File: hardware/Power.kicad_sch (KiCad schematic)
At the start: 1 part, among them J201 4090 USB-C

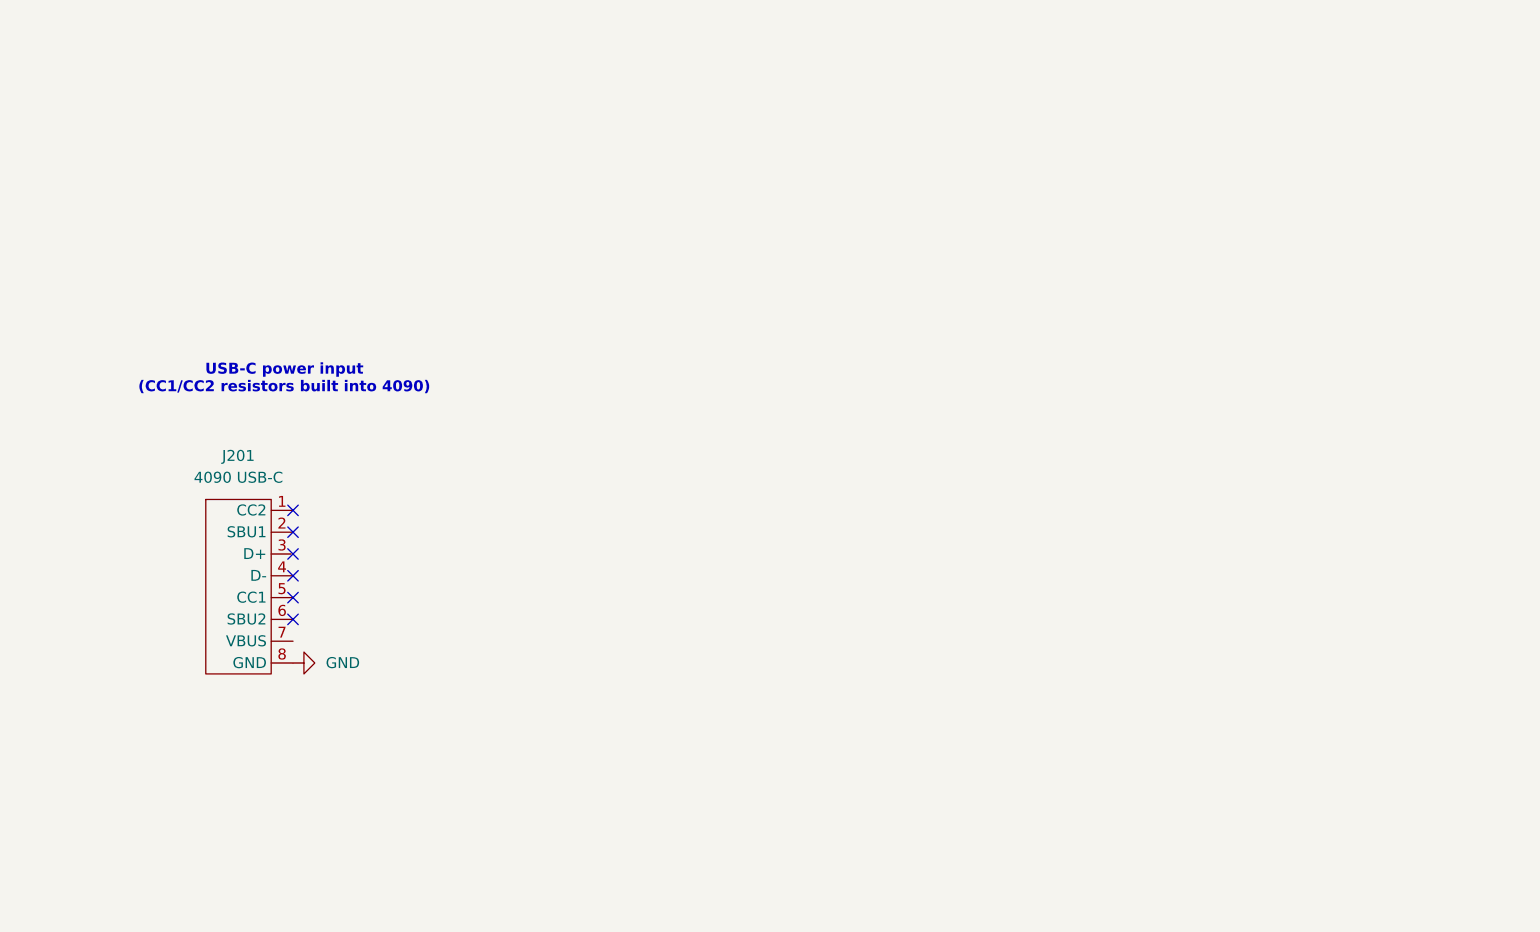
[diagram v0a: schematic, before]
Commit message: Complete schematics and component placements on board
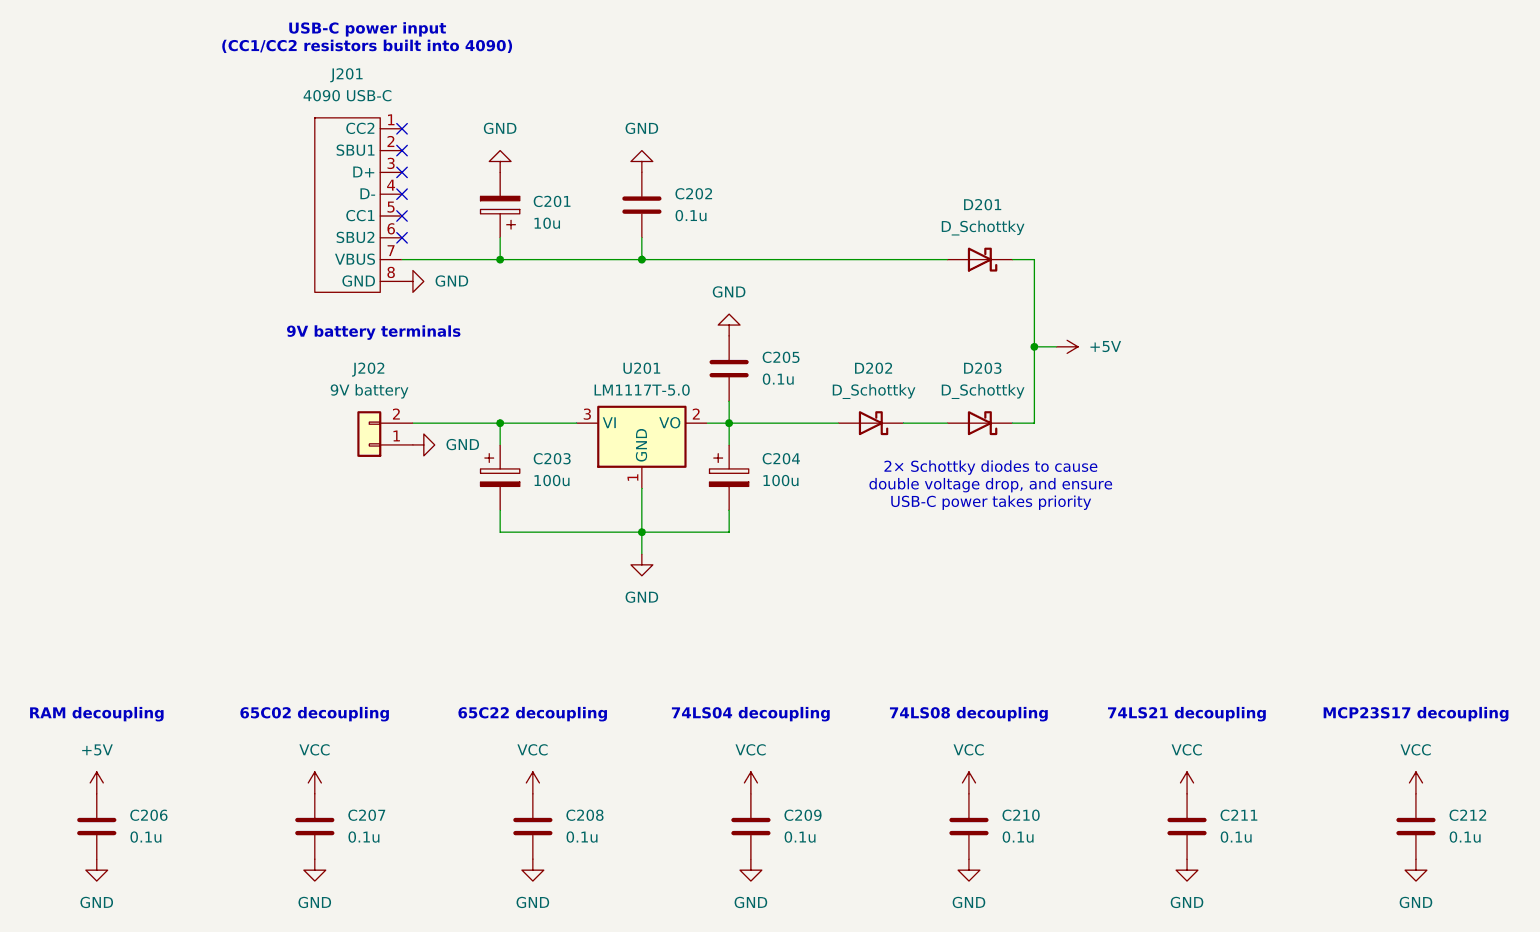
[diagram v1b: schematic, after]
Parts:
- added C201: 10u, Capacitor_THT:CP_Radial_D5.0mm_P2.00mm, symbol Device:C_Polarized
- added C202, C205, C206, C207, C208, C209, C210, C211, C212: 0.1u, Capacitor_THT:CP_Radial_D4.0mm_P1.50mm, symbol Device:C
- added C203, C204: 100u, Capacitor_THT:CP_Radial_D6.3mm_P2.50mm, symbol Device:C_Polarized
- added D201, D202, D203: D_Schottky, Diode_THT:D_DO-41_SOD81_P7.62mm_Horizontal, symbol Device:D_Schottky
- added J202: 9V battery, Connector_PinHeader_2.54mm:PinHeader_2x01_P2.54mm_Vertical, symbol Connector_Generic:Conn_01x02
- added U201: LM1117T-5.0, Package_TO_SOT_THT:TO-220-3_Horizontal_TabDown, symbol Regulator_Linear:LM1117T-5.0
- J201: footprint (none) -> Connector_PinHeader_2.54mm:PinHeader_1x08_P2.54mm_Vertical
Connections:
- net GND: now also C201.2, C202.1, C203.2, C204.2, C205.1, C206.2, C207.2, C208.2, C209.2, C210.2, C211.2, C212.2, J202.1 (Pin_1), U201.1 (GND)
- net at J201.7 (VBUS): now also C201.1, C202.2, D201.2 (A)
- new net: C203.1, J202.2 (Pin_2), U201.3 (VI)
- new net: D202.1 (K), D203.2 (A)
- new net: C204.1, C205.2, D202.2 (A), U201.2 (VO)
- new net +5V: C206.1, D201.1 (K), D203.1 (K)
- new net VCC: C207.1, C208.1, C209.1, C210.1, C211.1, C212.1
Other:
- note added: "2× Schottky diodes to cause double voltage drop, and ensure USB-C power takes priority"
- note added: "65C02 decoupling"
- note added: "65C22 decoupling"
- note added: "74LS04 decoupling"
- note added: "74LS08 decoupling"
- note added: "74LS21 decoupling"
- note added: "9V battery terminals"
- note added: "MCP23S17 decoupling"
- note added: "RAM decoupling"
- moved on the sheet: J201
